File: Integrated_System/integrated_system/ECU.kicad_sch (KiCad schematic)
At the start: 0 parts

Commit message: Added Components
Added esp32 and some transistors
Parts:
- added A1: Adafruit_Feather_HUZZAH32_ESP32, Module:Adafruit_Feather, symbol MCU_Module:Adafruit_Feather_HUZZAH32_ESP32
- added C1: 10u, symbol Device:C_Polarized_Small_US
- added C2: 1n, symbol Device:C_Small_US
- added J1: Jack-DC, symbol Connector:Jack-DC
- added U1: ~, symbol LM2596:LM2596
- added U2, U3, U4: IRLR7843, IRLR7843:TO252, symbol IRLR7843:IRLR7843
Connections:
- new net: A1.20 (A7/IO32), U3.1
- new net: A1.19 (A6/IO14), U2.1
- new net: A1.2 (3V3), U1.3 (Vout+)
- new net: A1.21 (A8/IO15), U4.1
- new net +12V: C1.1, C2.1, J1.1, U1.1 (Vin+), U2.3, U3.3, U4.3
- new net GND: A1.4 (GND), C1.2, C2.2, J1.2, U1.2 (Vin-), U1.4 (Vout-)
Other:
- company: (none) -> OSSEM
- title: (none) -> Integrated System

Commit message: Added Sensors
Made a bunch of changes
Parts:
- added D1, D2, D3: 1N4004, Diode_THT:D_DO-41_SOD81_P10.16mm_Horizontal, symbol Diode:1N4004
- added J2: Fan 1, symbol Connector:Screw_Terminal_01x02
- added J3: Fan 2, symbol Connector:Screw_Terminal_01x02
- added J4: Fan 3, symbol Connector:Screw_Terminal_01x02
- added RV1: Pot1, symbol Device:R_Potentiometer_Trim_US
- added U5: SCD30, SCD30:MODULE_SCD30, symbol SCD30:SCD30
- added U6: SGP30, SGP30:SGP30, symbol SGP30:SGP30
- added U7: SHT40-AD1F-R2, SHT40-AD1F-R2:SHT4X, symbol SHT40-AD1F-R2:SHT40-AD1F-R2
- U1: value ~ -> DC to DC Buck Converter 12V to 3.3V
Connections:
- net +12V: now also D1.1 (K), D2.1 (K), D3.1 (K), J2.2 (Pin_2), J3.2 (Pin_2), J4.2 (Pin_2); no longer U2.3, U3.3, U4.3
- net GND: now also U2.2, U3.2, U4.2, RV1.3, U5.2 (GND), U6.2 (VSS), U7.4 (VSS)
- net at A1.17 (SDA/IO23): now also U5.4 (RX/SDA), U6.3 (SDA), U7.1 (SDA)
- net at A1.18 (SCL/IO22): now also U5.3 (TX/SCL), U6.6 (SCL), U7.2 (SCL)
- net at A1.2 (3V3), U1.3 (Vout+): now also RV1.1
- net at A1.22 (A9/IO33): now also RV1.2
- new net: D3.2 (A), J4.1 (Pin_1), U4.3
- new net: D1.2 (A), J2.1 (Pin_1), U2.3
- new net: D2.2 (A), J3.1 (Pin_1), U3.3
- new net VDD: U5.1 (VDD), U6.1 (VDD), U7.3 (VDD)
- no-connect marks 0 -> 6
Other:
- note added: "VDD (+ 3.3 V)"
- moved on the sheet: A1, C1, C2, J1, U1, U2, U3, U4

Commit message: Added Notes
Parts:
- added R1, R2, R3: 100, symbol Device:R_Small_US
- added R4, R5, R6: 10k, symbol Device:R_Small_US
- C1: value 10u -> 100u
- C2: value 1n -> 0.1u
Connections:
- net GND: now also R4.1, R5.1, R6.1
- net at U3.1: now also R2.1, R5.2; no longer A1.20 (A7/IO32)
- net at U2.1: now also R1.1, R4.2; no longer A1.19 (A6/IO14)
- net at A1.21 (A8/IO15): now also R3.2; no longer U4.1
- new net: A1.19 (A6/IO14), R1.2
- new net: A1.20 (A7/IO32), R2.2
- new net: R3.1, R6.2, U4.1
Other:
- moved on the sheet: C1, C2

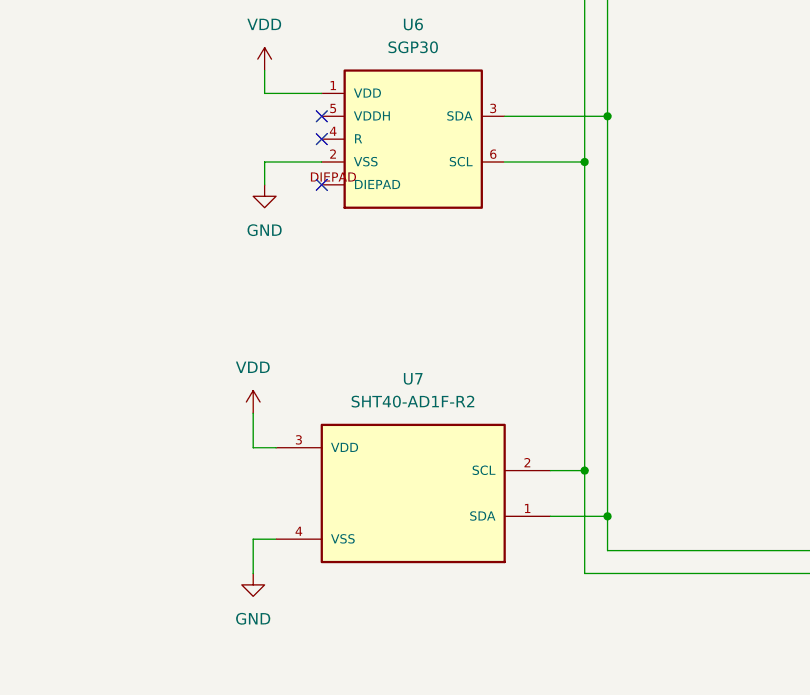
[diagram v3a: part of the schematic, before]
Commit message: changed to bme280
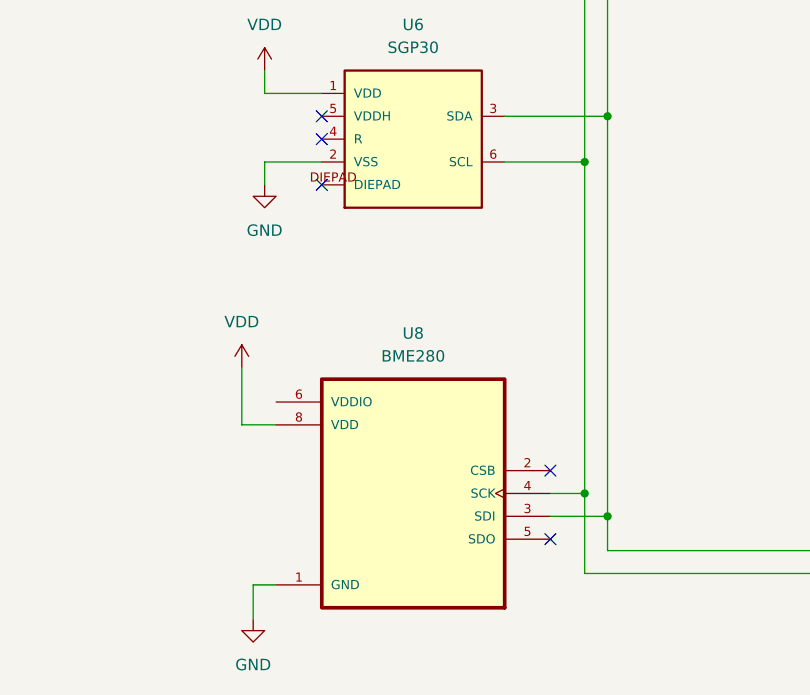
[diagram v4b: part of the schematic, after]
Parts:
- removed U7: SHT40-AD1F-R2, SHT40-AD1F-R2:SHT4X, symbol SHT40-AD1F-R2:SHT40-AD1F-R2
- added U8: BME280, BME280:PSON65P250X250X100-8N, symbol BME280:BME280
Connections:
- net GND: now also U8.1 (GND), U8.7 (GND)
- net VDD: now also U8.8 (VDD)
- net at A1.17 (SDA/IO23), U5.4 (RX/SDA), U6.3 (SDA): now also U8.3 (SDI)
- net at A1.18 (SCL/IO22), U5.3 (TX/SCL), U6.6 (SCL): now also U8.4 (SCK)
- no-connect marks 6 -> 8

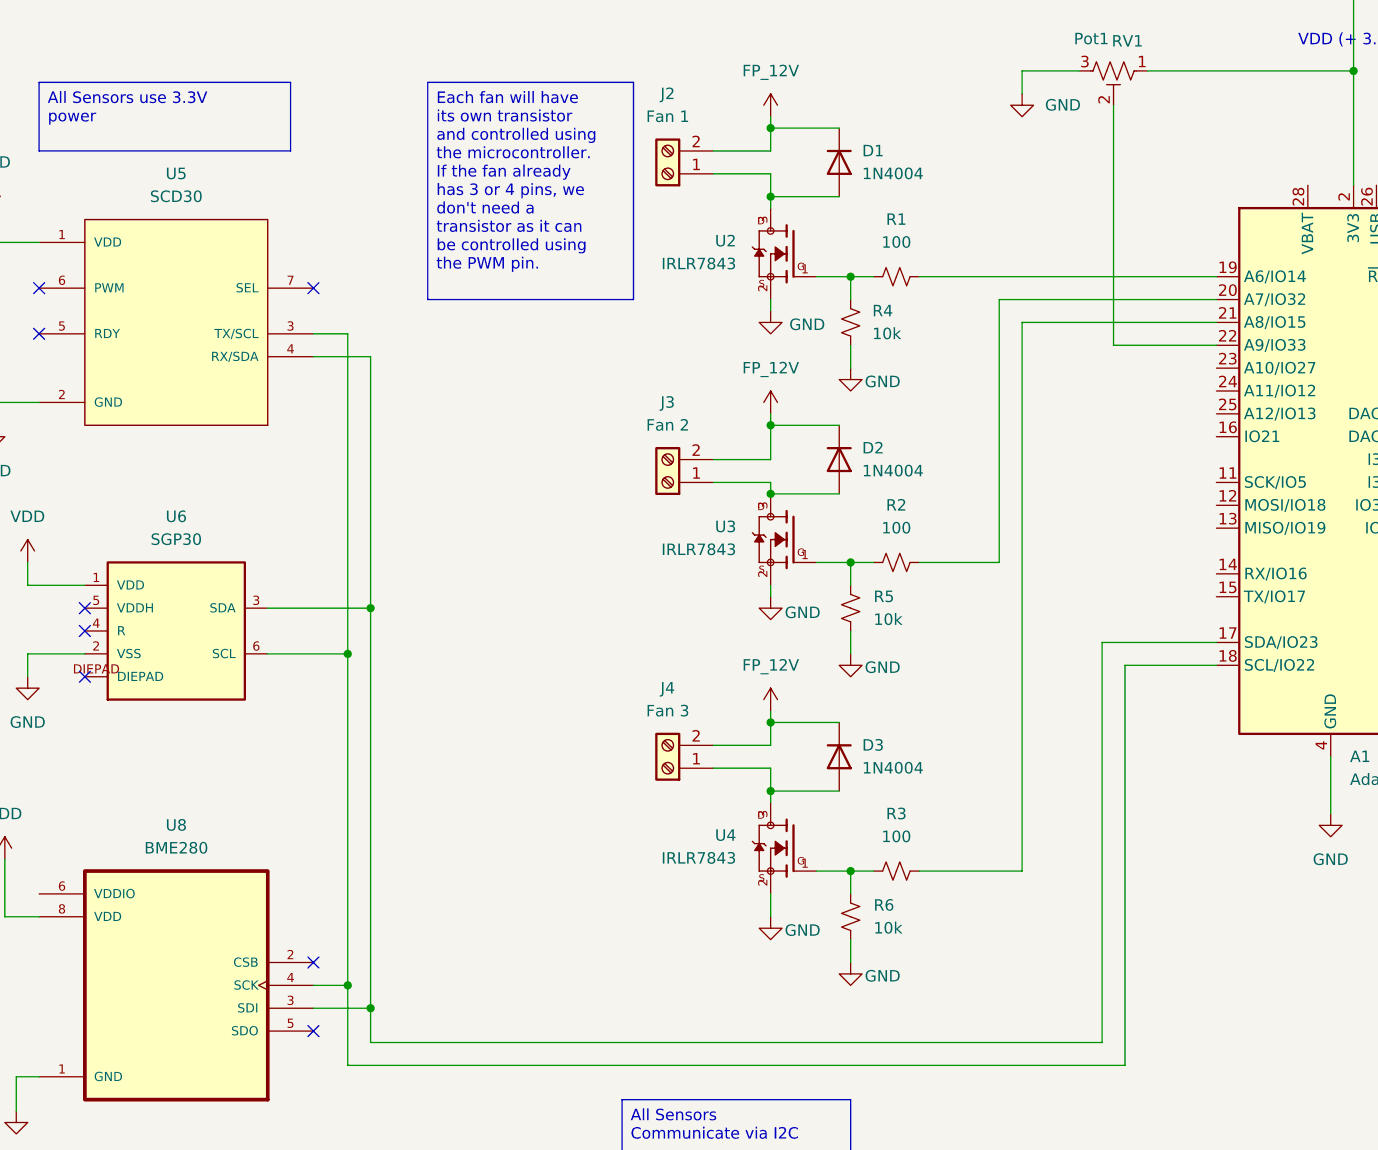
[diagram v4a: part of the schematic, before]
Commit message: replaced transistors
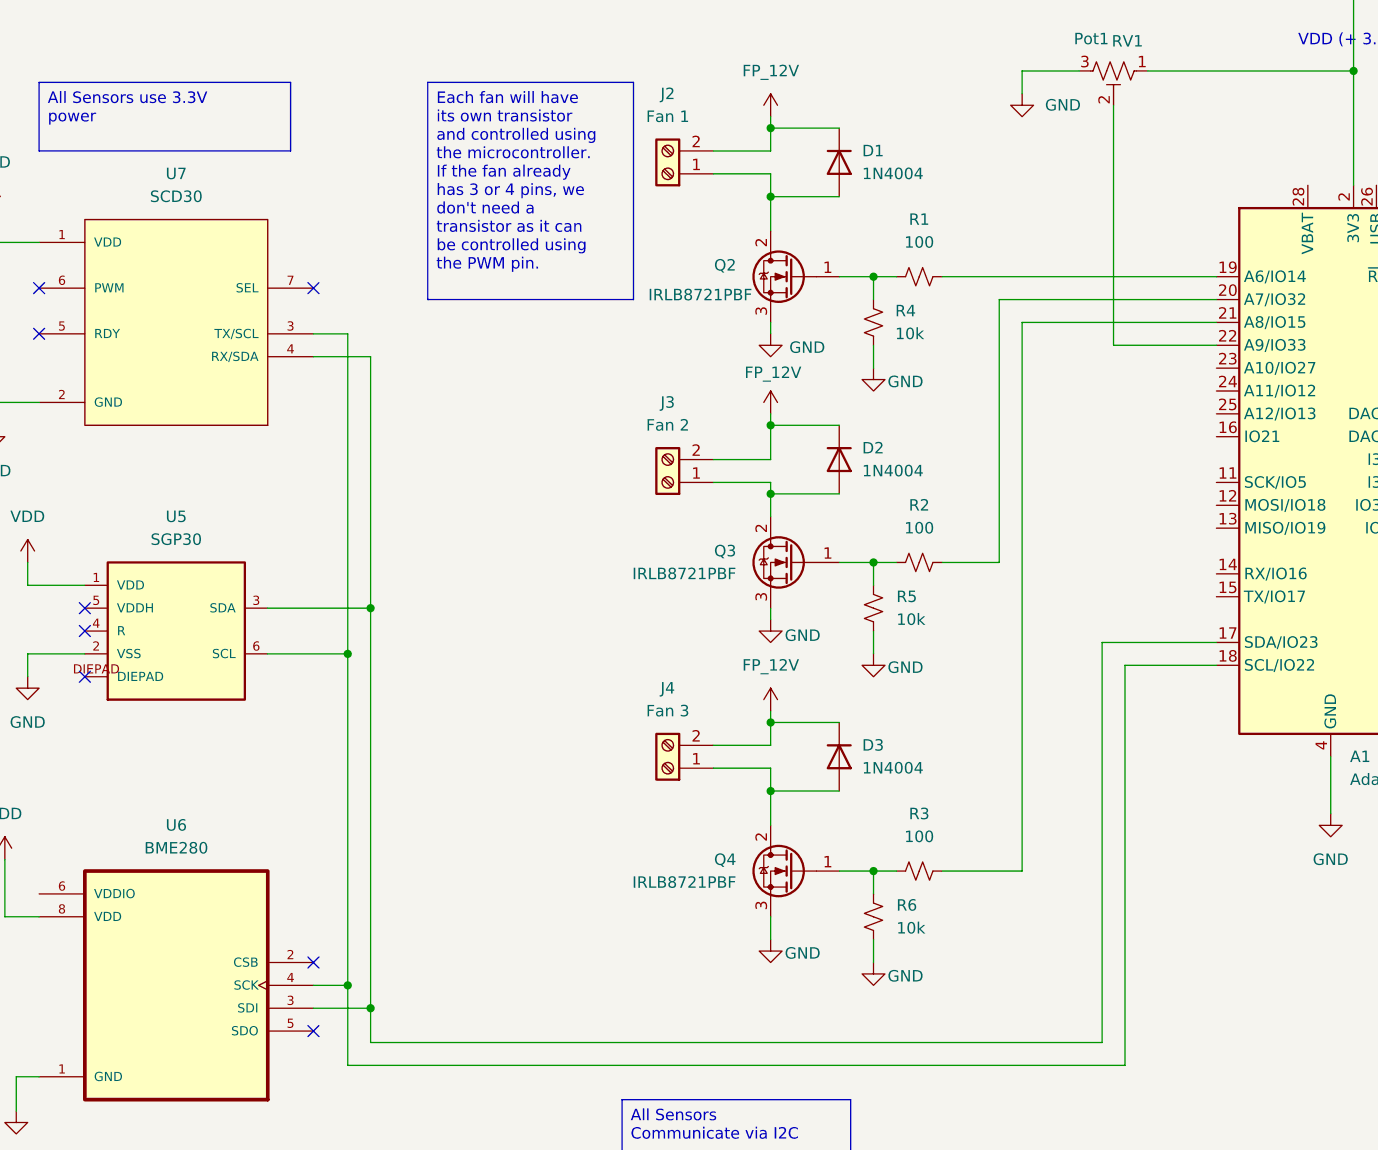
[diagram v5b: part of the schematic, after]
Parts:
- removed U2, U3, U4: IRLR7843, IRLR7843:TO252, symbol IRLR7843:IRLR7843
- removed U5: SCD30, SCD30:MODULE_SCD30, symbol SCD30:SCD30
- removed U6: SGP30, SGP30:SGP30, symbol SGP30:SGP30
- removed U8: BME280, BME280:PSON65P250X250X100-8N, symbol BME280:BME280
- added Q2, Q3, Q4: IRLB8721PBF, Package_TO_SOT_THT:TO-220-3_Vertical, symbol Transistor_FET:IRLB8721PBF
- added U5: SGP30, SGP30:SGP30, symbol SGP30:SGP30
- added U6: BME280, BME280:PSON65P250X250X100-8N, symbol BME280:BME280
- added U7: SCD30, SCD30:MODULE_SCD30, symbol SCD30:SCD30
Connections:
- net GND: now also Q2.3 (S), Q3.3 (S), Q4.3 (S), U5.2 (VSS), U6.1 (GND), U6.7 (GND), U7.2 (GND)
- net VDD: now also U5.1 (VDD), U6.8 (VDD), U7.1 (VDD)
- net at R1.1, R4.2: now also Q2.1 (G)
- net at D3.2 (A), J4.1 (Pin_1): now also Q4.2 (D)
- net at D1.2 (A), J2.1 (Pin_1): now also Q2.2 (D)
- net at A1.17 (SDA/IO23): now also U5.3 (SDA), U6.3 (SDI), U7.4 (RX/SDA)
- net at A1.18 (SCL/IO22): now also U5.6 (SCL), U6.4 (SCK), U7.3 (TX/SCL)
- net at R2.1, R5.2: now also Q3.1 (G)
- net at D2.2 (A), J3.1 (Pin_1): now also Q3.2 (D)
- net at R3.1, R6.2: now also Q4.1 (G)
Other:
- moved on the sheet: R1, R2, R3, R4, R5, R6

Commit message: Renamecomp
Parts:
- Q2, Q3, Q4: value IRLB8721PBF -> TN0702N3
- RV1: value Pot1 -> Pot1_Control
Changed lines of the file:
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@@
 		(on_board yes)
 		(dnp no)
-		(fields_autoplaced yes)
 		(property "Reference" "J2"
 			(at 115.57 68.58 0)
@@
 			)
 		)
-		(property "Value" "IRLB8721PBF"
+		(property "Value" "TN0702N3"
 			(at 124.968 90.932 0)
 			(effects
@@
 			)
 		)
-		(property "Value" "IRLB8721PBF"
+		(property "Value" "TN0702N3"
 			(at 123.19 156.2099 0)
 			(effects
@@
 			)
 		)
-		(property "Value" "IRLB8721PBF"
+		(property "Value" "TN0702N3"
 			(at 123.19 121.9199 0)
 			(effects
@@
 			)
 		)
-		(property "Value" "Pot1"
-			(at 164.592 62.484 90)
+		(property "Value" "Pot1_Control"
+			(at 162.56 62.484 90)
 			(effects
 				(font
